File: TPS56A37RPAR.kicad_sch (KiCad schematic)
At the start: 20 parts, among them U5 TPS56A37RPAR, U7 SPX3819M5-L

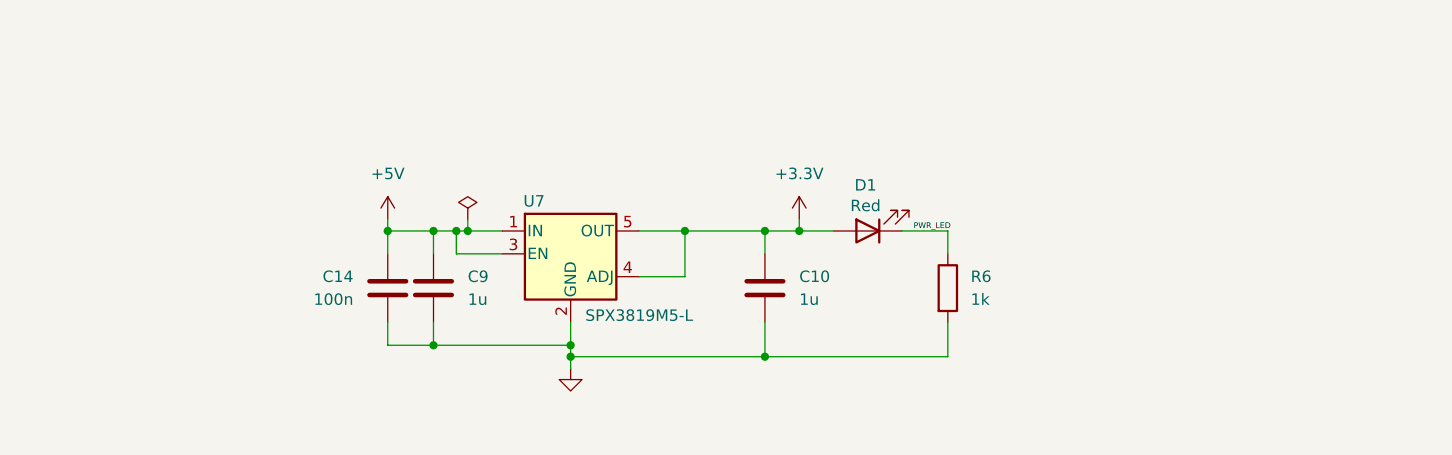
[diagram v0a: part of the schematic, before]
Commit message: Added extra LDO and pushed so Ireland can start to add Solenoids
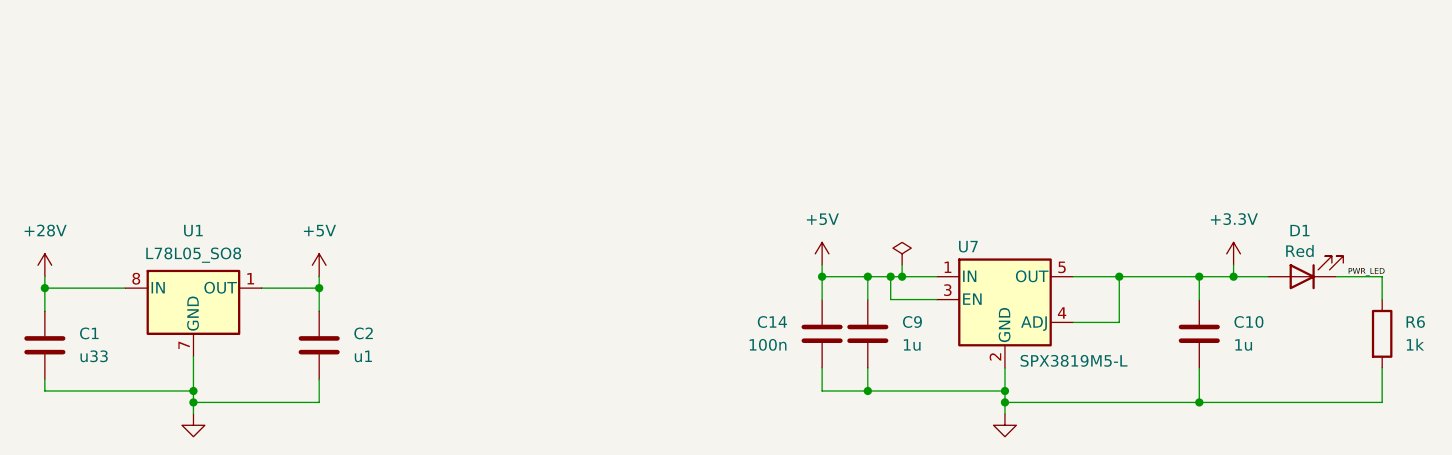
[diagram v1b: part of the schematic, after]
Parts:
- added C1: u33, symbol Device:C
- added C2: u1, symbol Device:C
- added U1: L78L05_SO8, Package_SO:SOIC-8_3.9x4.9mm_P1.27mm, symbol Regulator_Linear:L78L05_SO8
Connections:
- net +28V: now also C1.1, U1.8 (IN)
- net +5V: now also C2.1, U1.1 (OUT)
- net GND: now also C1.2, C2.2, U1.2 (GND), U1.3 (GND), U1.6 (GND), U1.7 (GND)
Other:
- moved on the sheet: C10, C14, C9, D1, R6, U7

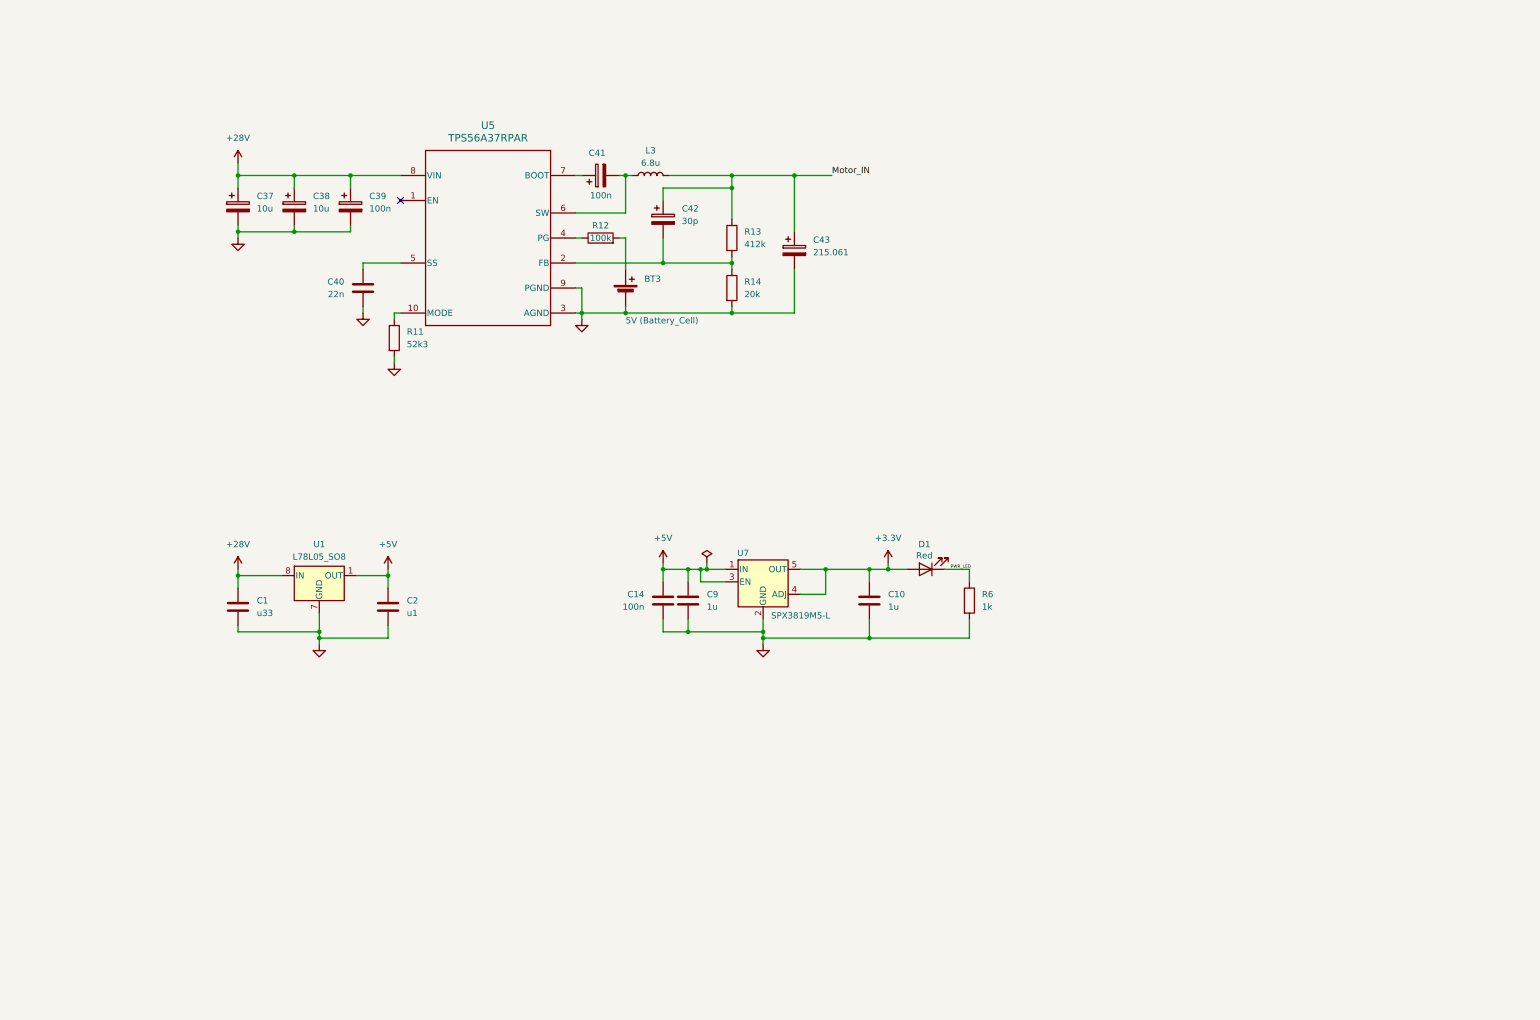
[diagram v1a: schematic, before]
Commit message: Changes before syncing to main. Adding crystal as well as Thermocouple sensor and buck 3.3V step down
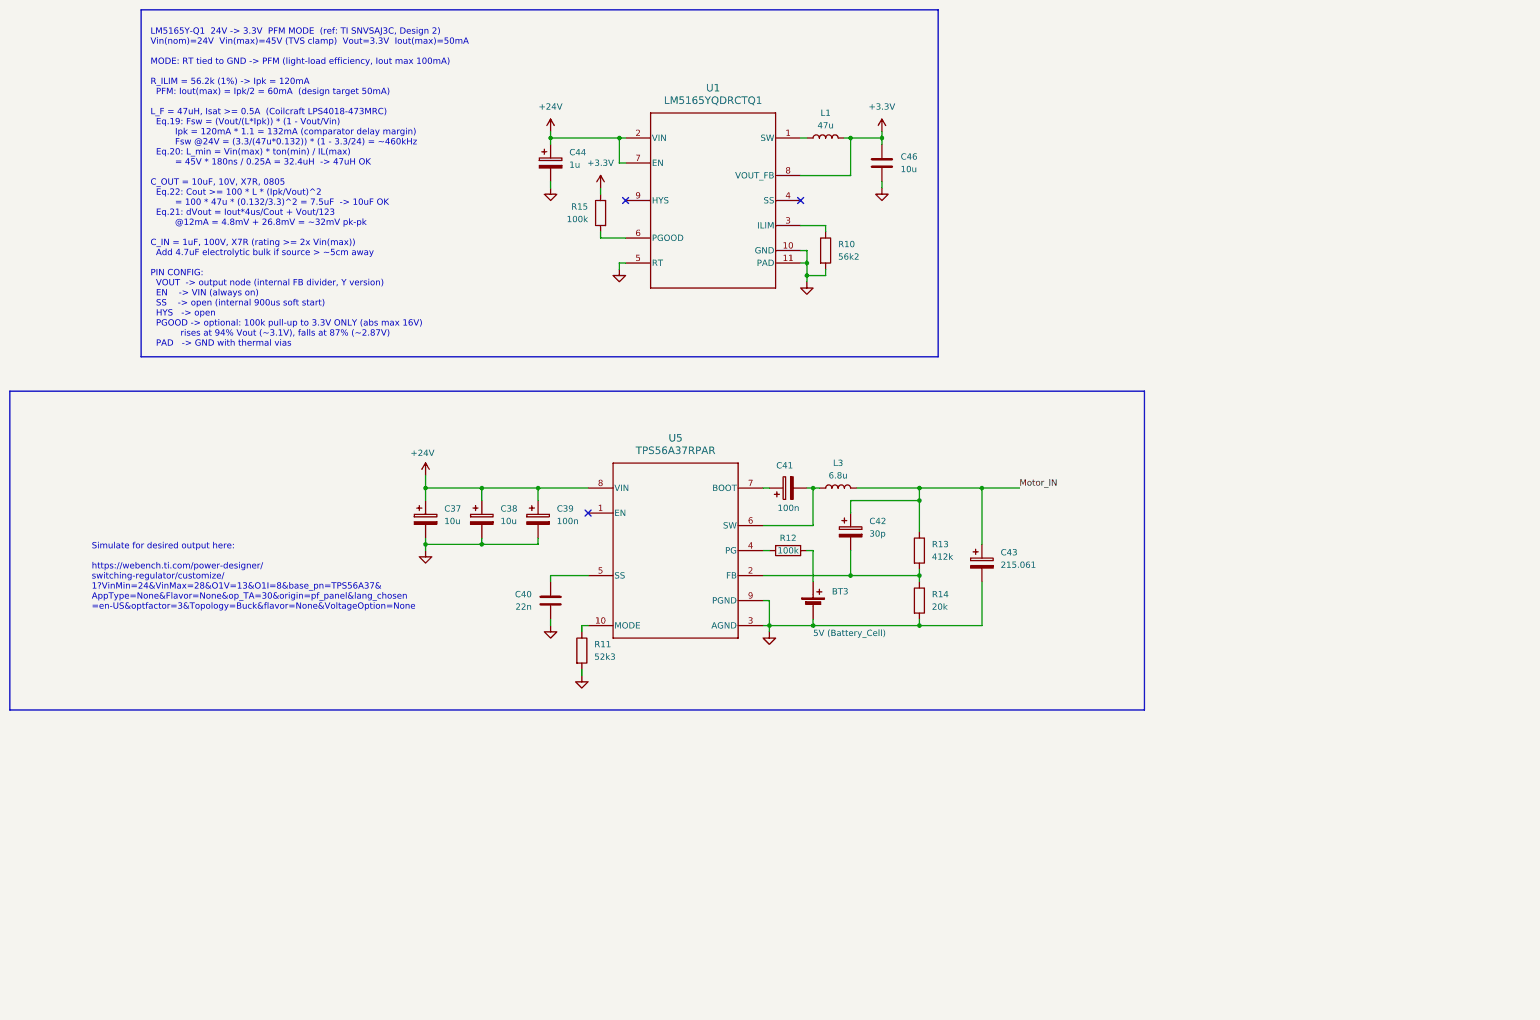
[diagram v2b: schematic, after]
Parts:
- removed C1: u33, symbol Device:C
- removed C10, C9: 1u, Capacitor_SMD:C_0603_1608Metric, symbol Device:C
- removed C14: 100n, Capacitor_SMD:C_0402_1005Metric, symbol Device:C
- removed C2: u1, symbol Device:C
- removed D1: Red, LED_SMD:LED_0603_1608Metric, symbol Device:LED
- removed R6: 1k, Resistor_SMD:R_0402_1005Metric, symbol Device:R
- removed U1: L78L05_SO8, Package_SO:SOIC-8_3.9x4.9mm_P1.27mm, symbol Regulator_Linear:L78L05_SO8
- removed U7: SPX3819M5-L, Package_TO_SOT_SMD:SOT-23-5, symbol Regulator_Linear:SPX3819M5-L
- added C44: 1u, symbol Device:C_Polarized
- added C46: 10u, symbol Device:C
- added L1: 47u, symbol Device:L
- added R10: 56k2, Resistor_SMD:R_0402_1005Metric, symbol Device:R
- added R15: 100k, Resistor_SMD:R_0402_1005Metric, symbol Device:R
- added U1: LM5165YQDRCTQ1, DRC0010J, symbol Imported_ICs:LM5165YQDRCTQ1
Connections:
- net +3.3V: now also C46.2, L1.2, R15.1, U1.8 (VOUT_FB)
- net GND: now also C44.2, C46.1, R10.2, U1.10 (GND), U1.11 (PAD), U1.5 (RT)
- net +28V renamed +24V
- net +24V: now also C44.1, U1.2 (VIN), U1.7 (EN)
- new net: R15.2, U1.6 (PGOOD)
- new net: L1.1, U1.1 (SW)
- new net: R10.1, U1.3 (ILIM)
- no-connect marks 1 -> 3
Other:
- note added: "LM5165Y-Q1 24V -> 3.3V PFM MODE (ref: TI SNVSAJ3C, Design 2) Vin(nom)=24V Vin(max)=45V (TVS clamp) Vout=3.3V Iout(max)=50mA MODE: RT tied to GND -> PFM (light-load efficiency, Iout max 100mA) R_ILIM = 56.2k (1%) -> Ipk = 120mA PFM: Iout(max) = Ipk/2 = 60mA (design target 50mA) L_F = 47uH, Isat >= 0.5A (Coilcraft LPS4018-473MRC) Eq.19: Fsw = (Vout/(L*Ipk)) * (1 - Vout/Vin) Ipk = 120mA * 1.1 = 132m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"
- note added: "Simulate for desired output here: https://webench.ti.com/power-designer/ switching-regulator/customize/ 1?VinMin=24&VinMax=28&O1V=13&O1I=8&base_pn=TPS56A37& AppType=None&Flavor=None&op_TA=30&origin=pf_panel&lang_chosen =en-US&optfactor=3&Topology=Buck&flavor=None&VoltageOption=None"
- moved on the sheet: BT3, C37, C38, C39, C40, C41, C42, C43, L3, R11, R12, R13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

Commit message: added npn in so that GPIO can be 5V or roughly 0V
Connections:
- net +5V: now reaches BT3.1 (+), R12.2
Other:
- moved on the sheet: BT3, C37, C38, C39, C40, C41, C42, C43, C44, C46, L1, L3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

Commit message: Added changes to pass ERC check
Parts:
- renumbered BT3 to BT1, C37 to C1, C38 to C2, C39 to C3, C40 to C4, C41 to C5, C44 to C6, C42 to C7, C43 to C8, C46 to C9, L3 to L1, L1 to L2, R11 to R1, R12 to R2, R15 to R3, R13 to R4, R14 to R5, R10 to R6, U5 to U1, U1 to U2
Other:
- moved on the sheet: C9, L2

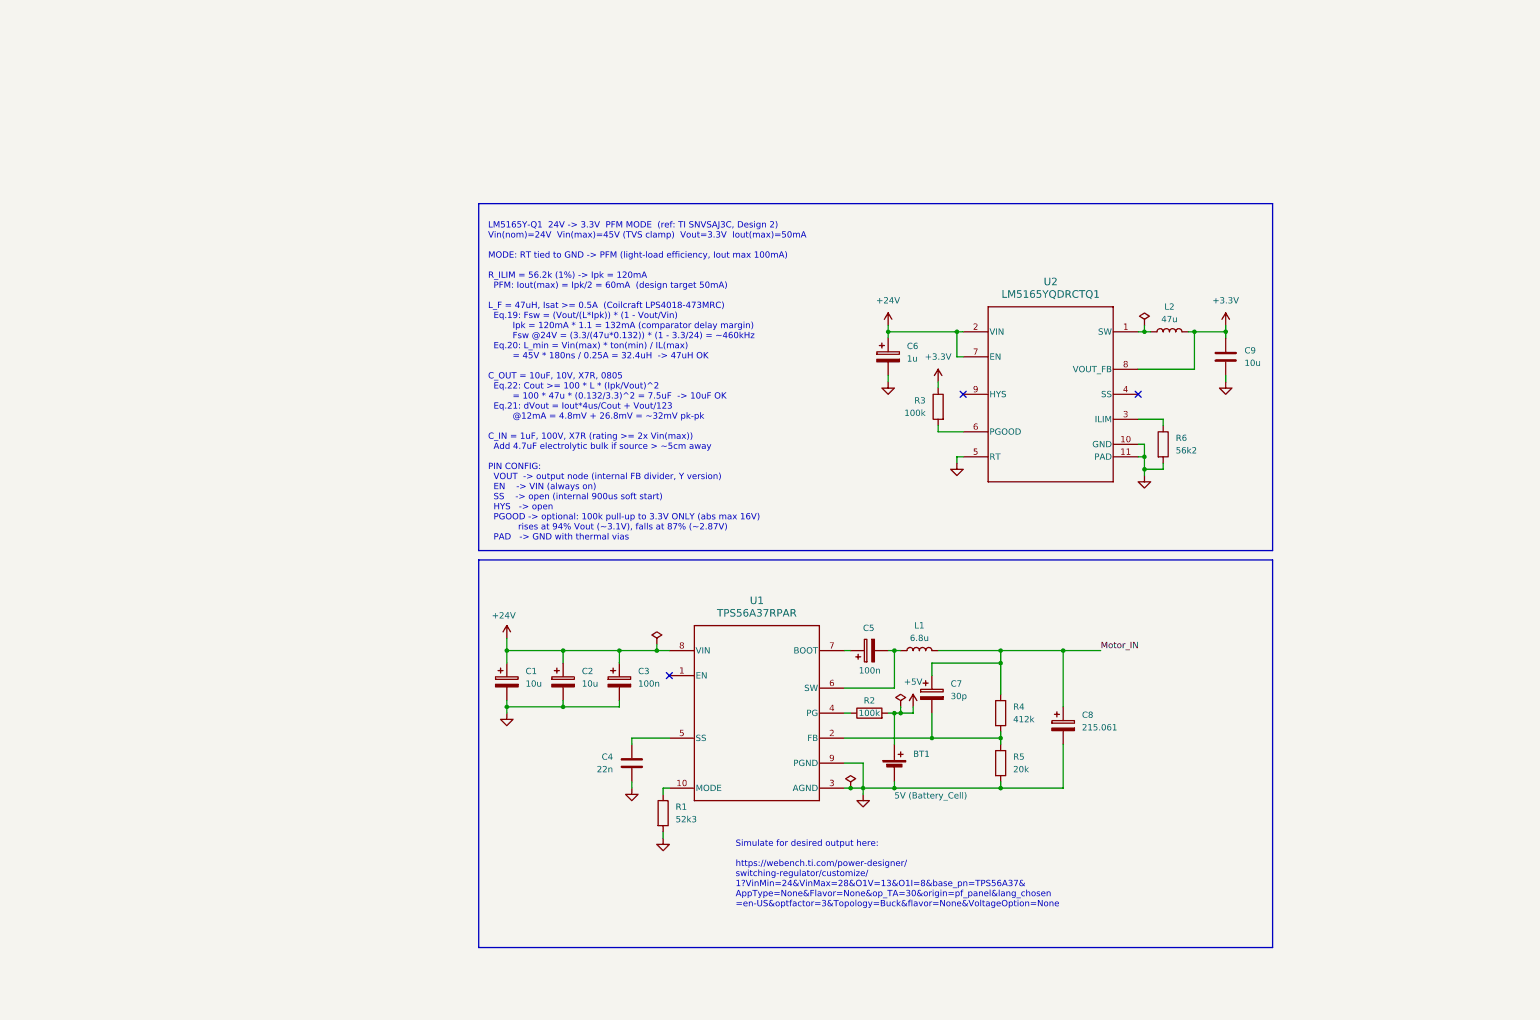
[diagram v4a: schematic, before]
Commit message: added footprints to every component except inductors. That will be in the next commit
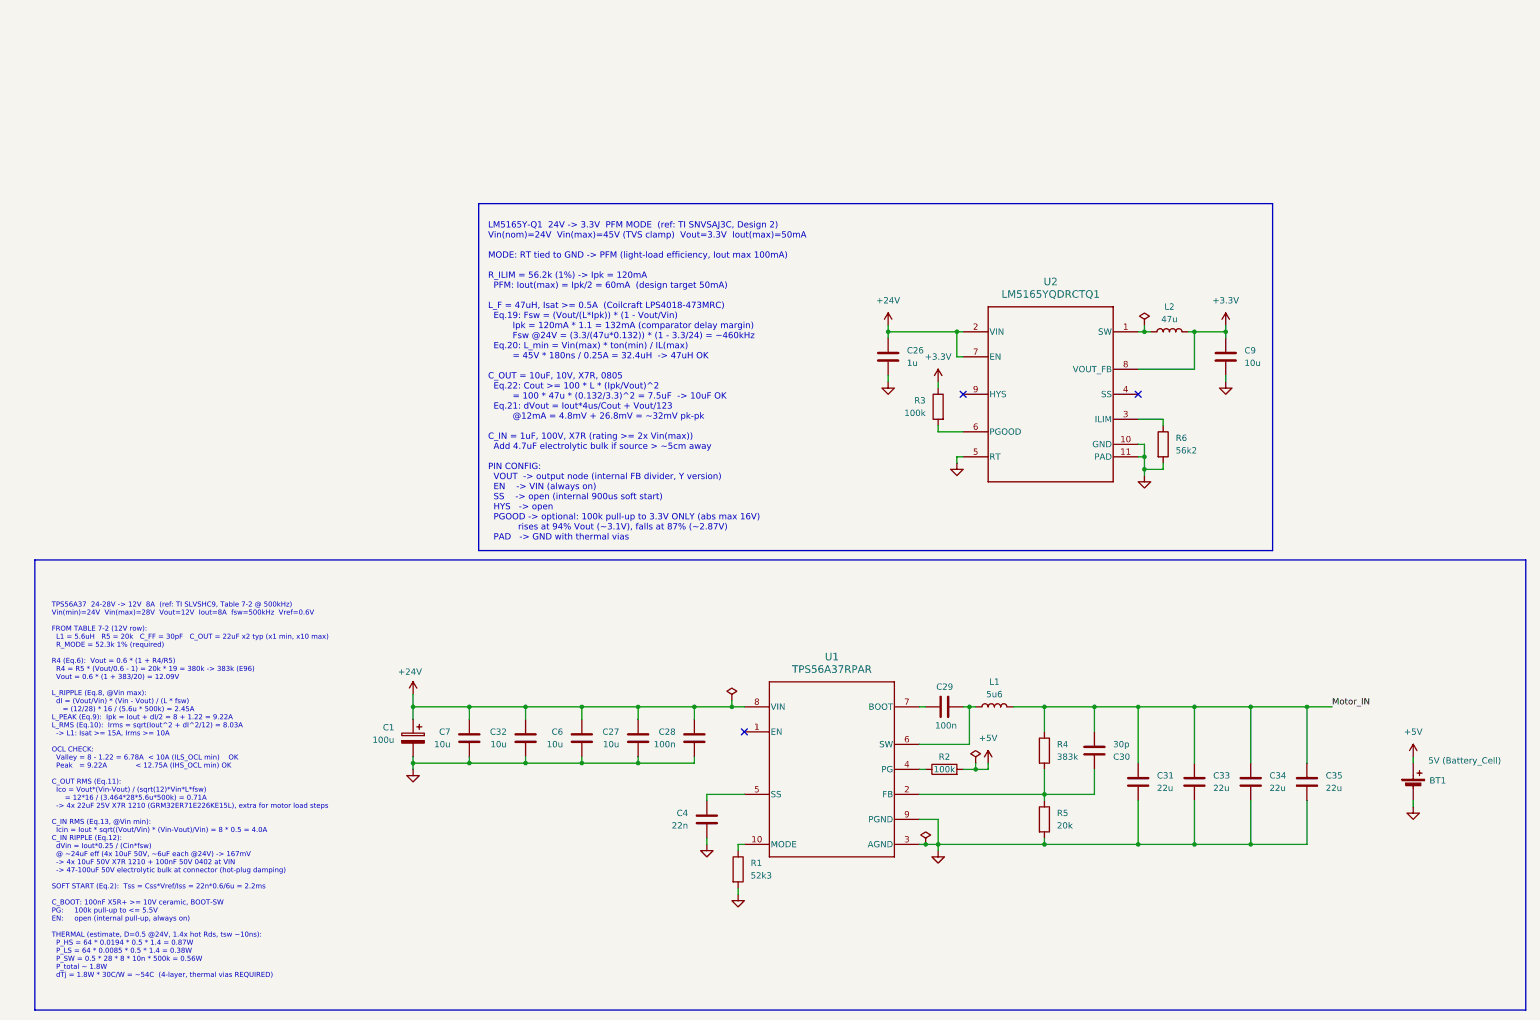
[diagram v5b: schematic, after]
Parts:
- removed C2: 10u, symbol Device:C_Polarized
- removed C3, C5: 100n, symbol Device:C_Polarized
- removed C6: 1u, symbol Device:C_Polarized
- removed C7: 30p, symbol Device:C_Polarized
- removed C8: 215.061, symbol Device:C_Polarized
- added C26: 1u, Capacitor_SMD:C_0805_2012Metric, symbol Device:C
- added C27, C32, C6, C7: 10u, Capacitor_SMD:C_1210_3225Metric, symbol Device:C
- added C28: 100n, Capacitor_SMD:C_1210_3225Metric, symbol Device:C
- added C29: 100n, Capacitor_SMD:C_0805_2012Metric, symbol Device:C
- added C30: 30p, Capacitor_SMD:C_0402_1005Metric, symbol Device:C
- added C31, C33, C34, C35: 22u, Capacitor_SMD:C_1210_3225Metric, symbol Device:C
- C1: value 10u -> 100u; footprint (none) -> Library:CHEMI-KE0
- C4, C9: footprint (none) -> Capacitor_SMD:C_0402_1005Metric
- L1: value 6.8u -> 5u6
- R1, R2, R5: footprint (none) -> Resistor_SMD:R_0402_1005Metric
- R4: value 412k -> 383k; footprint (none) -> Resistor_SMD:R_0402_1005Metric
- U1: footprint RPA0010A-MFG -> Library:RPA0010A-MFG
- U2: footprint DRC0010J -> Library:DRC0010J
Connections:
- net +24V: now also C26.2, C27.2, C28.2, C32.2, C6.2, C7.2
- net GND: now also C26.1, C27.1, C28.1, C31.1, C32.1, C33.1, C34.1, C35.1, C6.1, C7.1
- net Motor_IN: now also C30.1, C31.2, C33.2, C34.2, C35.2
- net at R4.2, R5.1, U1.2 (FB): now also C30.2
- net at U1.7 (BOOT): now also C29.2
- net at L1.1, U1.6 (SW): now also C29.1
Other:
- note added: "TPS56A37 24-28V -> 12V 8A (ref: TI SLVSHC9, Table 7-2 @ 500kHz) Vin(min)=24V Vin(max)=28V Vout=12V Iout=8A fsw=500kHz Vref=0.6V FROM TABLE 7-2 (12V row): L1 = 5.6uH R5 = 20k C_FF = 30pF C_OUT = 22uF x2 typ (x1 min, x10 max) R_MODE = 52.3k 1% (required) R4 (Eq.6): Vout = 0.6 * (1 + R4/R5) R4 = R5 * (Vout/0.6 - 1) = 20k * 19 = 380k -> 383k (E96) Vout = 0.6 * (1 + 383/20) = 12.09V L_RIPPLE (Eq.8, @V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"
- note removed: "Simulate for desired output here: https://webench.ti.com/power-designer/ switching-regulator/customize/ 1?VinMin=24&VinMax=28&O1V=13&O1I=8&base_pn=TPS56A37& AppType=None&Flavor=None&op_TA=30&origin=pf_panel&lang_chosen =en-US&optfactor=3&Topology=Buck&flavor=None&VoltageOption=None"
- moved on the sheet: C4, L1, R1, R2, R4, R5, U1
